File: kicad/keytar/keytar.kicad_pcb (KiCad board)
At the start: 2 copper layers, 70 x 90 mm, 40 parts, among them J1 , J2 USB_B, J3 AudioJack2, J4 Conn_01x04, J5 USB_A, J6 Mini-DIN-6-Shielded, J7 Conn_01x04, Q1 BSS138, Q2 BSS138, SW1 SW_DPST_x2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

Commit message: kicad: finalize pcb design for order
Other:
- board text added: "Keytar V2 design by AberDerBart"

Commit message: add traces to read charger status
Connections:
- net Net-(D2-A) renamed /5V_MIDI
- net Net-(D3-A) renamed /5V_USB
- U1 pad 19: unconnected-(U1-GPIO14-Pad19) -> CHARGE STATE
- U1 pad 20: unconnected-(U1-GPIO15-Pad20) -> STANDBY STATE
- U2 pad 6: unconnected-(U2-STDBY-Pad6) -> STANDBY STATE
- U2 pad 7: unconnected-(U2-CHRG-Pad7) -> CHARGE STATE
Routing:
- net STANDBY STATE: track 0.00 -> 96.1 mm, vias 0 -> 1
- net CHARGE STATE: track 0.00 -> 93.1 mm, vias 0 -> 1

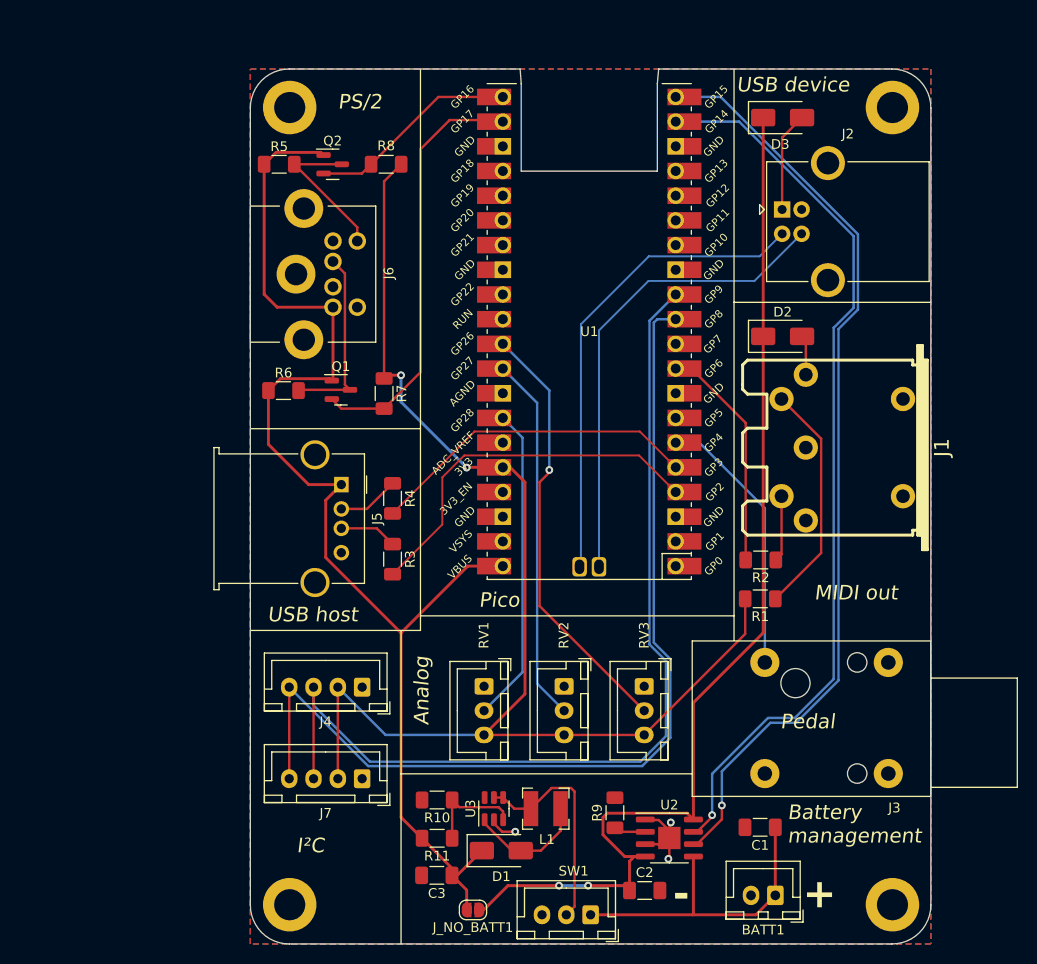
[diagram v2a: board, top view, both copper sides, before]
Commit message: kicad: use proper capacitors
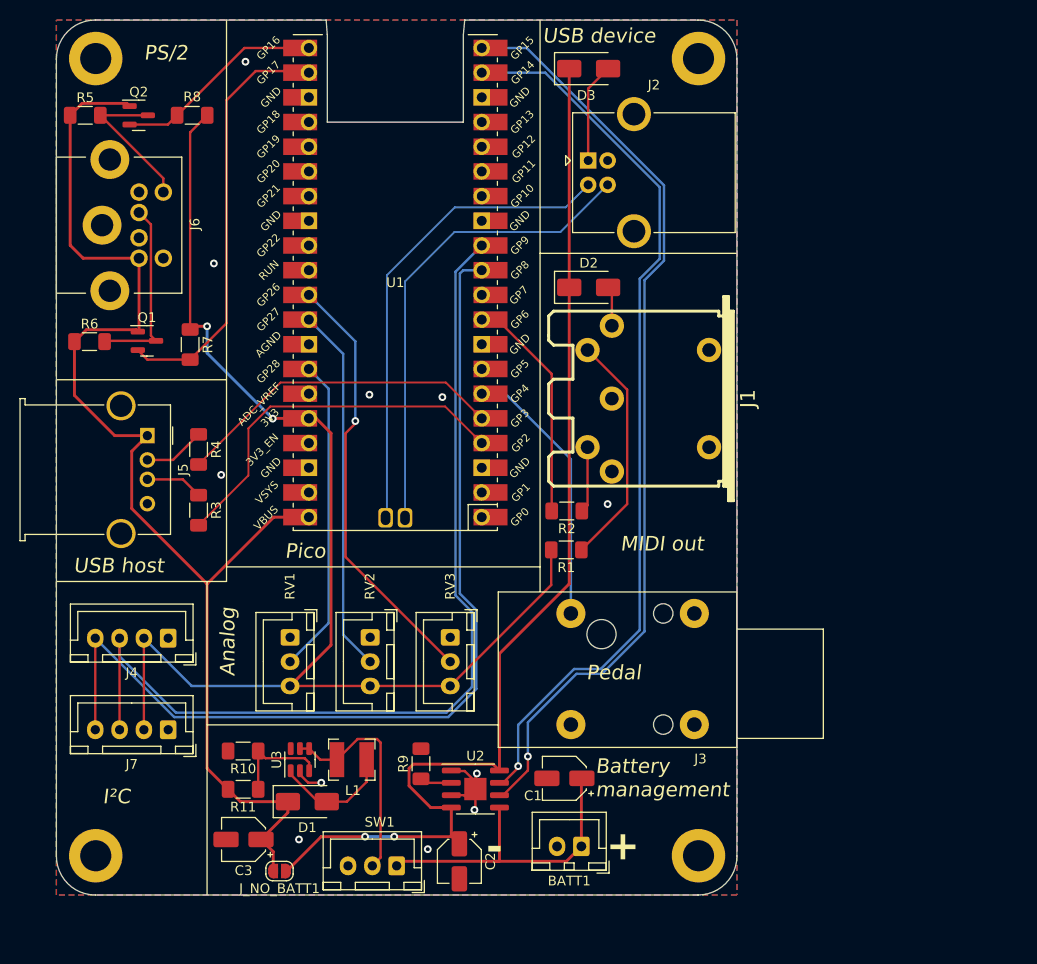
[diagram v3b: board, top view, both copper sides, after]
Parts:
- C1, C2, C3: footprint Capacitor_SMD:C_1206_3216Metric_Pad1.33x1.80mm_HandSolder -> Capacitor_SMD:CP_Elec_4x5.3
- moved C1 20.8 mm to (152.3, 128.0)
- moved J1 20.6 mm to (160.1, 88.9)
- moved J3 20.6 mm to (152.9, 111.0)
- moved RV3 20.6 mm to (140.5, 113.5)
- moved J5 20.6 mm to (109.4, 92.8)
- moved R10 20.6 mm to (119.2, 125.2)
- moved R11 20.6 mm to (119.2, 129.1)
- moved R6 20.6 mm to (103.4, 83.1)
- moved J2 20.6 mm to (154.7, 64.5)
- moved J4 20.6 mm to (111.5, 113.6)
- moved J6 20.6 mm to (100.0, 71.1)
- moved L1 20.6 mm to (130.4, 126.1)
- moved Q2 20.6 mm to (108.5, 59.8)
- moved R5 20.6 mm to (103.0, 59.8)
- moved R8 20.6 mm to (114.0, 59.8)
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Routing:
- net VBUS: track 113.5 -> 116.8 mm
- net +5V: track 125.1 -> 127.1 mm
- net GND: vias 3 -> 11

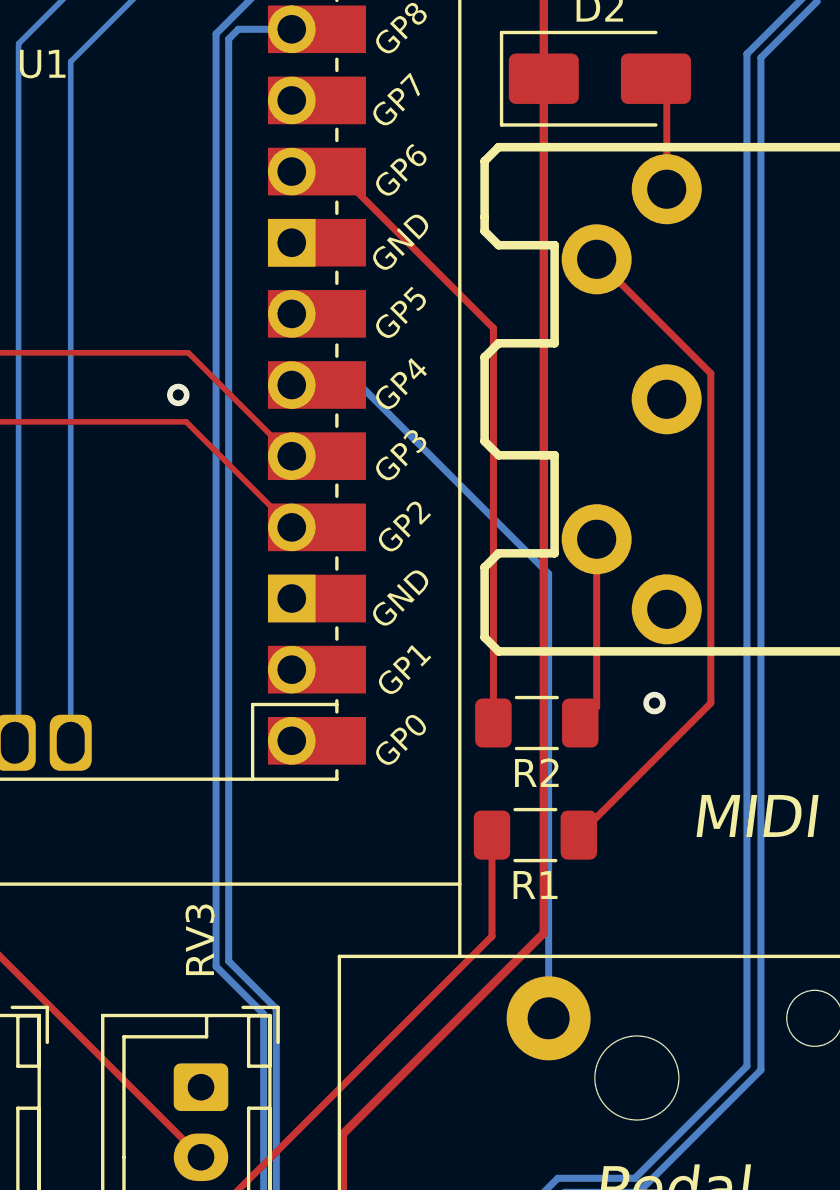
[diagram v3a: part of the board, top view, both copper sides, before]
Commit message: pcb: adjust midi and pedal pins
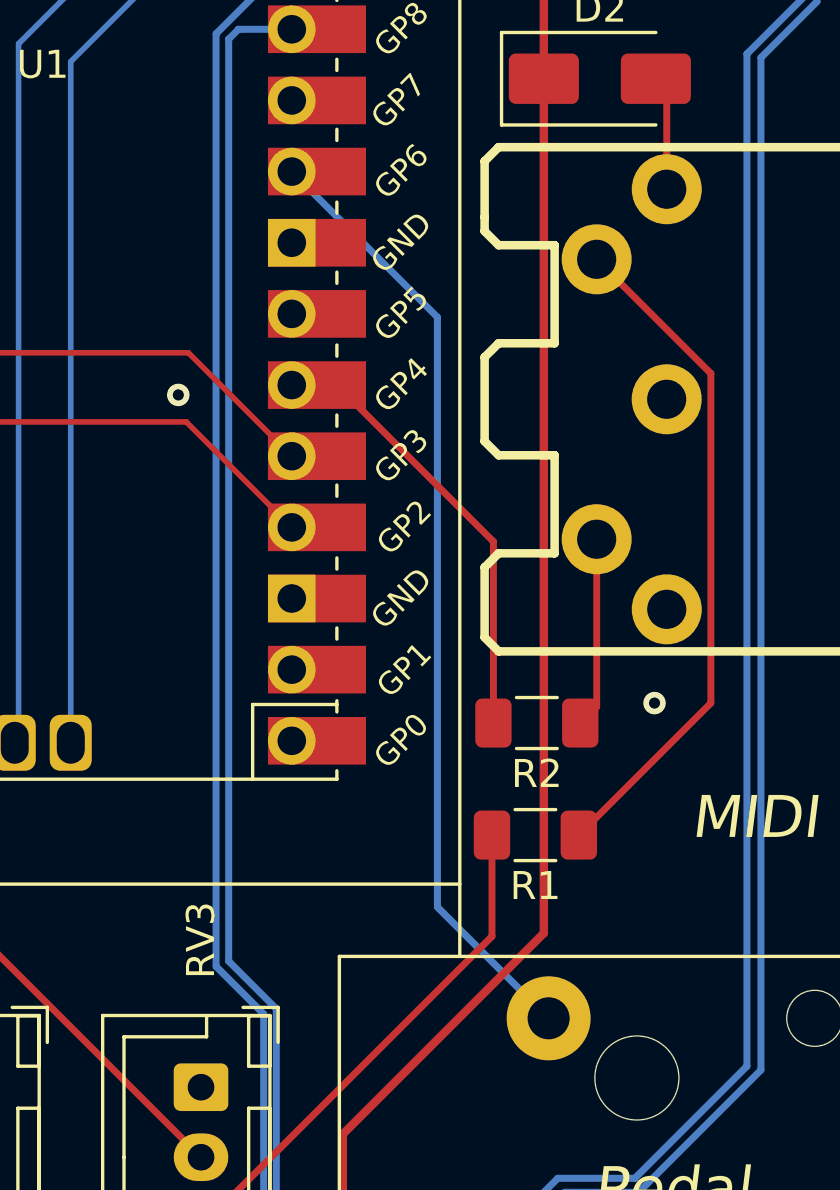
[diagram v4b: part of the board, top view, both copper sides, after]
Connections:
- U1 pad 6: PEDAL -> MIDI TX
- U1 pad 9: MIDI TX -> PEDAL
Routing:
- net PEDAL: track 27.8 -> 34.0 mm
- net MIDI TX: track 22.0 -> 16.0 mm
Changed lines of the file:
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@@
       (net 54 "USB HOST D-") (pinfunction "GPIO3") (pintype "bidirectional"))
     (pad "6" thru_hole oval (at -8.89 -11.43 180) (size 1.7 1.7) (drill 1.02) (layers "*.Cu" "*.Mask")
-      (net 51 "PEDAL") (pinfunction "GPIO4") (pintype "bidirectional"))
+      (net 10 "MIDI TX") (pinfunction "GPIO4") (pintype "bidirectional"))
     (pad "6" smd rect (at -8.89 -11.43 180) (size 3.5 1.7) (drill (offset -0.9 0)) (layers "F.Cu" "F.Mask")
-      (net 51 "PEDAL") (pinfunction "GPIO4") (pintype "bidirectional"))
+      (net 10 "MIDI TX") (pinfunction "GPIO4") (pintype "bidirectional"))
     (pad "7" thru_hole oval (at -8.89 -8.89 180) (size 1.7 1.7) (drill 1.02) (layers "*.Cu" "*.Mask")
       (net 16 "unconnected-(U1-GPIO5-Pad7)") (pinfunction "GPIO5") (pintype "bidirectional"))
@@
       (net 4 "GND") (pinfunction "GND") (pintype "power_in"))
     (pad "9" thru_hole oval (at -8.89 -3.81 180) (size 1.7 1.7) (drill 1.02) (layers "*.Cu" "*.Mask")
-      (net 10 "MIDI TX") (pinfunction "GPIO6") (pintype "bidirectional"))
+      (net 51 "PEDAL") (pinfunction "GPIO6") (pintype "bidirectional"))
     (pad "9" smd rect (at -8.89 -3.81 180) (size 3.5 1.7) (drill (offset -0.9 0)) (layers "F.Cu" "F.Mask")
-      (net 10 "MIDI TX") (pinfunction "GPIO6") (pintype "bidirectional"))
+      (net 51 "PEDAL") (pinfunction "GPIO6") (pintype "bidirectional"))
     (pad "10" thru_hole oval (at -8.89 -1.27 180) (size 1.7 1.7) (drill 1.02) (layers "*.Cu" "*.Mask")
       (net 18 "unconnected-(U1-GPIO7-Pad10)") (pinfunction "GPIO7") (pintype "bidirectional"))
@@
   (segment (start 103.0845 81.8535) (end 108.1785 81.8535) (width 0.3) (layer "F.Cu") (net 9))
   (segment (start 106 92.75) (end 101.8595 88.6095) (width 0.3) (layer "F.Cu") (net 9))
-  (segment (start 150.95 100.5) (end 150.95 86.4025) (width 0.25) (layer "F.Cu") (net 10))
-  (segment (start 150.95 86.4025) (end 145.362 80.8145) (width 0.25) (layer "F.Cu") (net 10))
+  (segment (start 150.95 100.5) (end 150.95 94.0225) (width 0.25) (layer "F.Cu") (net 10))
+  (segment (start 145.362 88.4345) (end 143.752 88.4345) (width 0.25) (layer "F.Cu") (net 10))
+  (segment (start 150.95 94.0225) (end 145.362 88.4345) (width 0.25) (layer "F.Cu") (net 10))
   (segment (start 124.0375 116) (end 128 112.0375) (width 0.25) (layer "B.Cu") (net 11))
   (segment (start 128 112.0375) (end 128 87.9225) (width 0.25) (layer "B.Cu") (net 11))
@@
   (via (at 134.75 134) (size 0.8) (drill 0.4) (layers "F.Cu" "B.Cu") (net 48))
   (segment (start 134.75 134) (end 131.75 134) (width 0.3) (layer "B.Cu") (net 48))
-  (segment (start 146.1845 88.4345) (end 152.921 95.171) (width 0.25) (layer "B.Cu") (net 51))
-  (segment (start 143.752 88.4345) (end 146.1845 88.4345) (width 0.25) (layer "B.Cu") (net 51))
-  (segment (start 152.921 95.171) (end 152.921 111.0405) (width 0.25) (layer "B.Cu") (net 51))
+  (segment (start 148.951 107.0705) (end 152.921 111.0405) (width 0.25) (layer "B.Cu") (net 51))
+  (segment (start 148.951 86.0135) (end 148.951 107.0705) (width 0.25) (layer "B.Cu") (net 51))
+  (segment (start 143.752 80.8145) (end 148.951 86.0135) (width 0.25) (layer "B.Cu") (net 51))
   (segment (start 122 89.75) (end 139.9875 89.75) (width 0.2) (layer "F.Cu") (net 53))
   (segment (start 119.75 96.8455) (end 119.75 92) (width 0.2) (layer "F.Cu") (net 53))

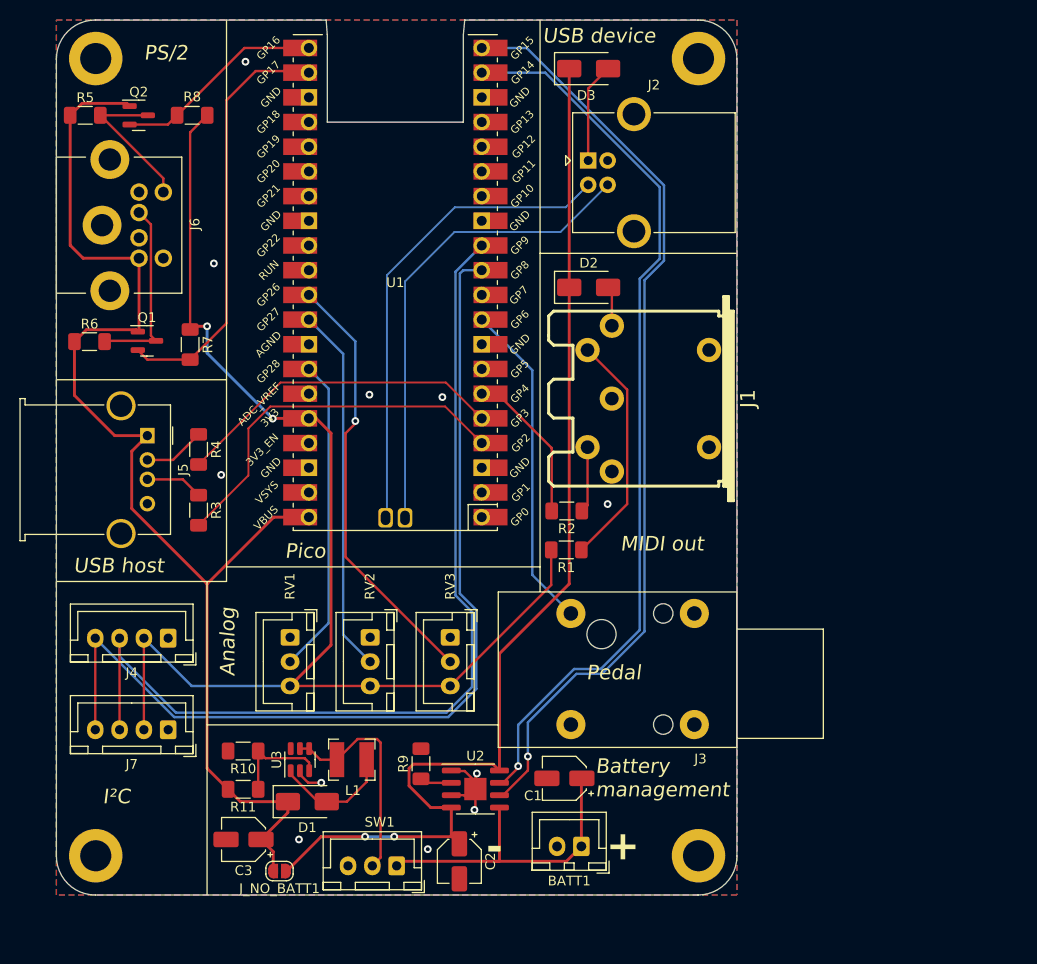
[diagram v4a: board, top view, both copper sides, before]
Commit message: pcb: switch usb device and host pins
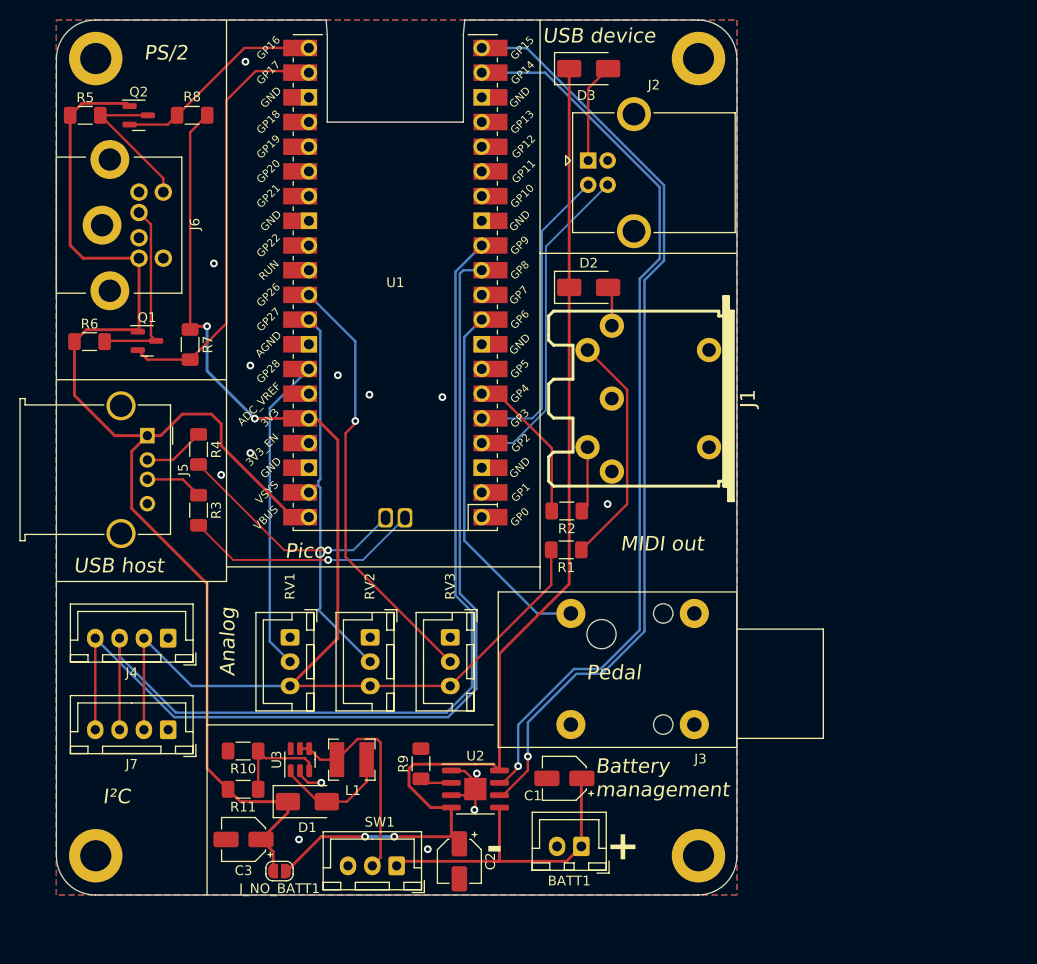
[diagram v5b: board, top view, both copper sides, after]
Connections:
- U1 pad 4: USB HOST D+ -> USB DEV D+
- U1 pad 44: USB DEV D- -> USB HOST D-
- U1 pad 45: USB DEV D+ -> USB HOST D+
- U1 pad 5: USB HOST D- -> USB DEV D-
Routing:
- net USB DEV D-: track 49.6 -> 31.6 mm
- net USB DEV D+: track 49.3 -> 33.8 mm
- net USB HOST D+: track 38.6 -> 24.5 mm, vias 0 -> 1
- net USB HOST D-: track 34.1 -> 24.3 mm, vias 0 -> 1
- net +5V: track 127.1 -> 135.2 mm
- net PEDAL: track 34.0 -> 37.5 mm
- net MIDI TX: track 16.0 -> 14.4 mm
- net VBUS: track 116.8 -> 115.6 mm
- net GND: track 12.2 -> 11.0 mm, vias 11 -> 14
- net +3V3: track 132.6 -> 133.8 mm
- net /5V_MIDI: track 4.65 -> 3.56 mm
- net +BATT: track 32.7 -> 32.0 mm
